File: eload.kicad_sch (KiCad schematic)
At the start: 5 parts, among them J1 Barrel_Jack, Q1 IRF740, U1 MAX4080T

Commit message: Schematics updated
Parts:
- removed U1: MAX4080T, symbol Amplifier_Current:MAX4080T
- added C1, C2, C3: 100nF, symbol Device:C_Small
- added R2: 330K, symbol Device:R_Small
- added R3: 100K, symbol Device:R_Small
- added U1: MCP4725, Package_TO_SOT_SMD:SOT-23-6, symbol Analog_DAC:MCP4725xxx-xCH
- added U2: AD2829, symbol Device:Opamp_Dual
- added U3: STM32F103C8Tx, Package_QFP:LQFP-48_7x7mm_P0.5mm, symbol MCU_ST_STM32F1:STM32F103C8Tx
- R1: symbol Device:R -> Device:R_Small
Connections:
- net Earth: now also R1.2, C1.2, C2.2, C3.2, R3.2, U1.2 (VSS), U1.6 (A0), U2.4 (V-); no longer Q1.3 (S)
- net VCC: now also C1.1, C2.1, C3.1, U1.3 (VDD), U2.8 (V+)
- net VDD: now also Q1.2 (D), R2.1; no longer R1.1
- net at Q1.1 (G): now also U2.1
- new net: Q1.3 (S), R1.1, U2.2 (-)
- new net: U3.23 (VSS), U3.35 (VSS), U3.47 (VSS)
- new net JNRST: U3.7 (NRST)
- new net SCL: U1.5 (SCL), U3.45 (PB8)
- new net SDA: U1.4 (SDA), U3.46 (PB9)
- new net SWCLK: U3.37 (PA14)
- new net SWDIO: U3.34 (PA13)
- new net Vctrl: U1.1 (VOUT), U2.3 (+)
- new net Vsense: R2.2, R3.1, U3.10 (PA0)
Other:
- note added: "15V MAX 12bit ADC 1bit/mV = 4.096V 1:4 division"
- note added: "Voltage Sensing & Current Regulation"
- note removed: "20V/V Gain 1A * 0.1R * 20V/V = 2V max"
- company: (none) -> Denis Bazhenov
- title: (none) -> Bench Electronic Load
- moved on the sheet: HS1, Q1, R1

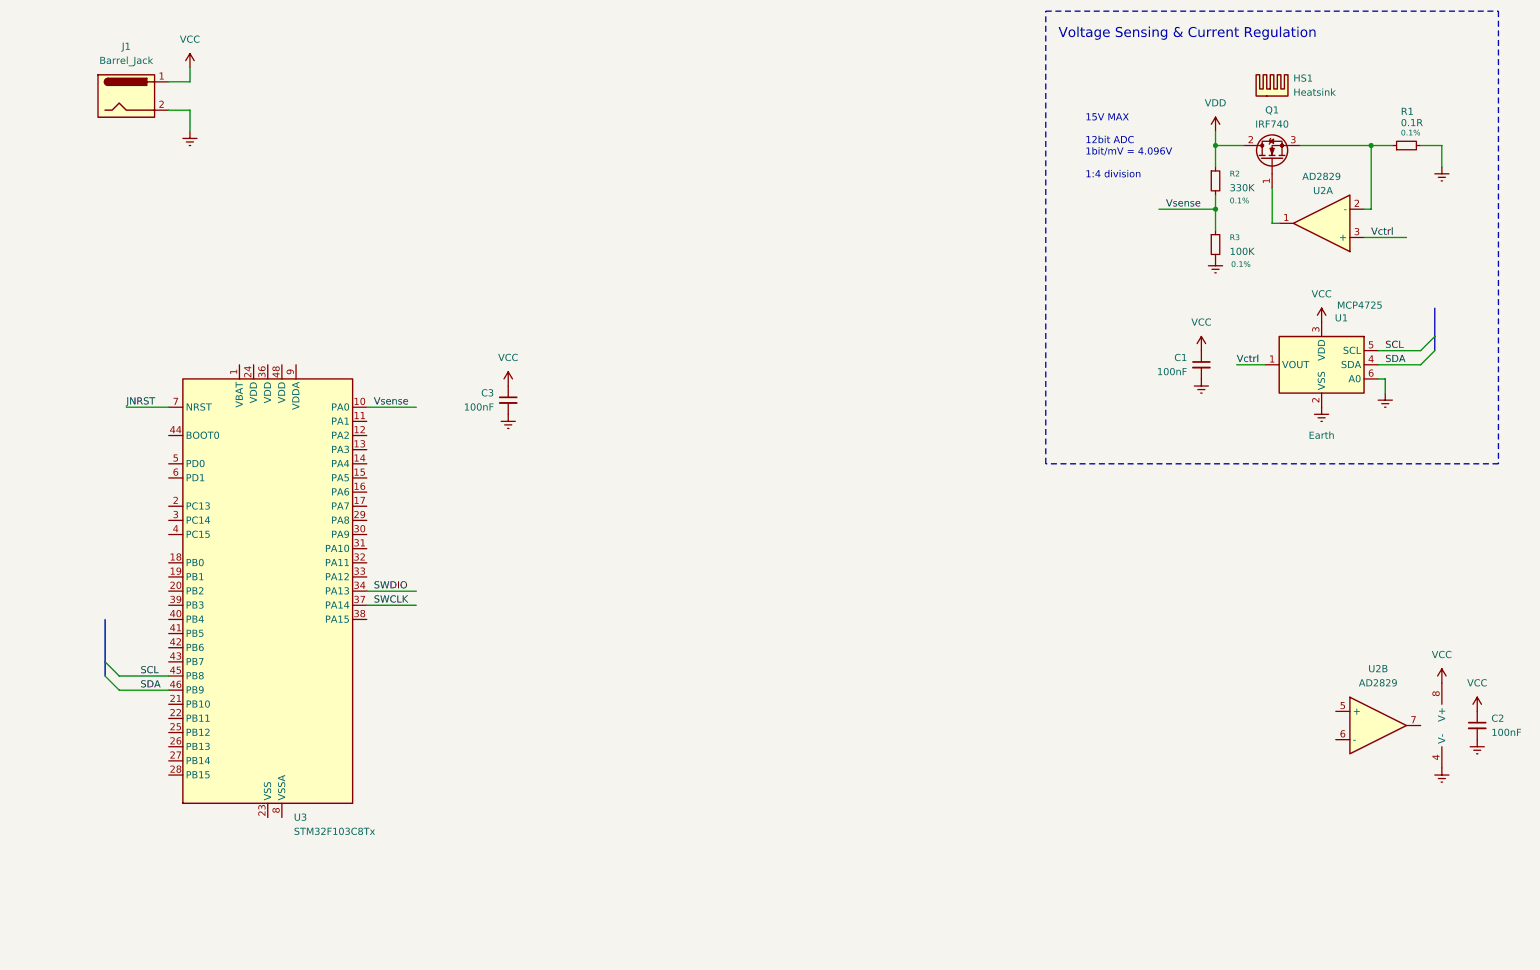
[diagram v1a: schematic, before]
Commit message: Schematics - Power Rail
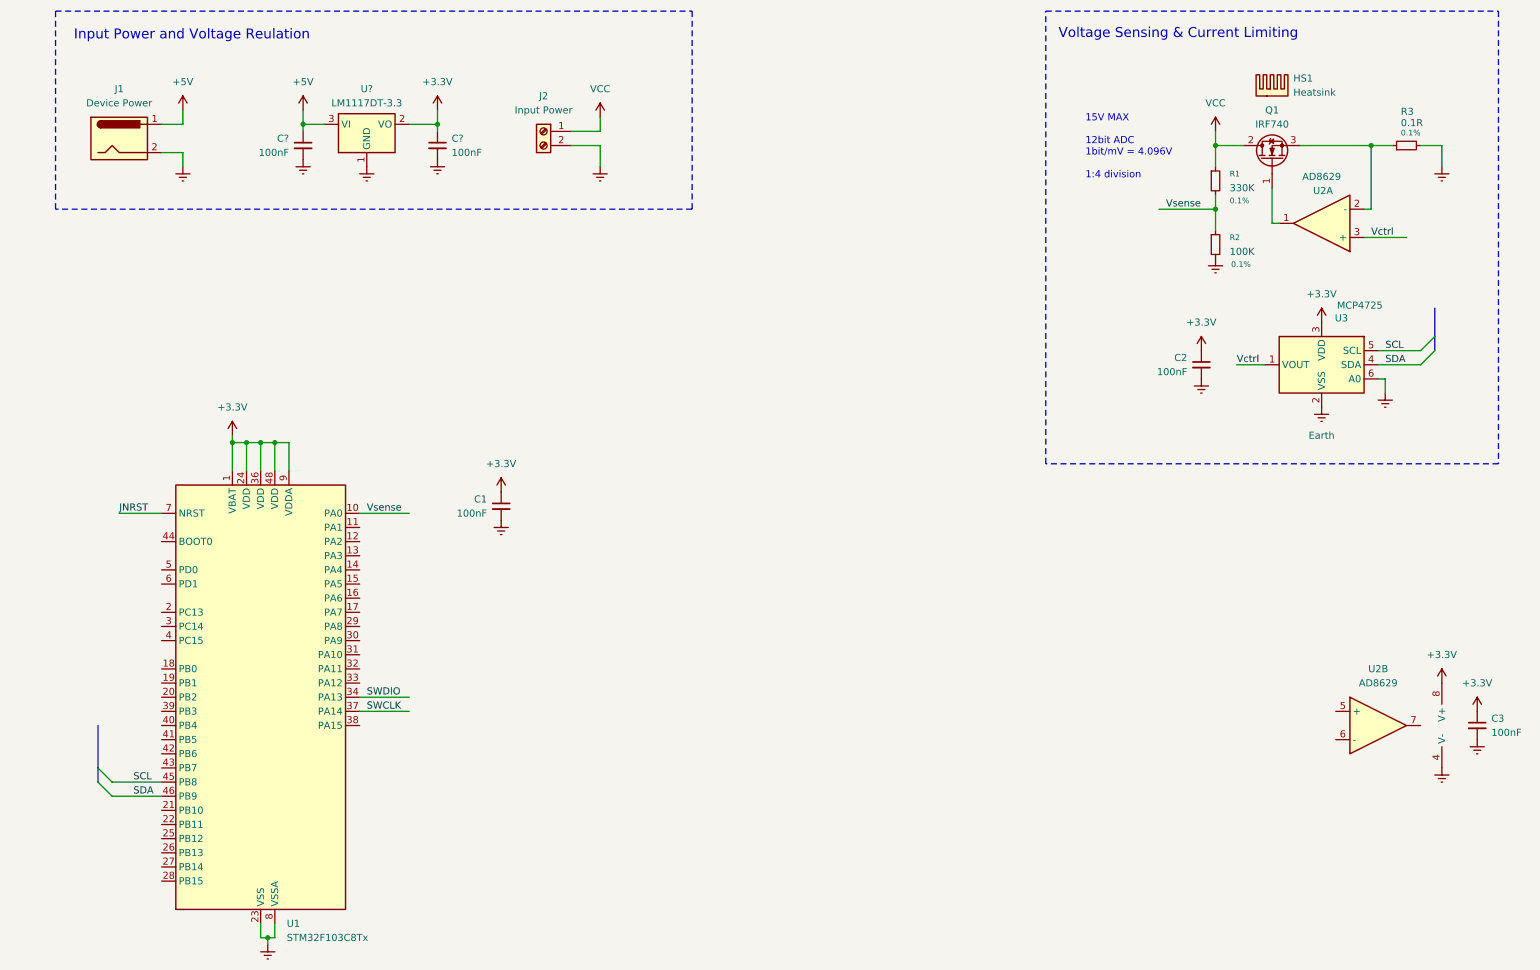
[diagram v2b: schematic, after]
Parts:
- added C? (x2): 100nF, symbol Device:C_Small
- added J2: Input Power, symbol Connector:Screw_Terminal_01x02
- added U?: LM1117DT-3.3, Package_TO_SOT_SMD:TO-252-2, symbol Regulator_Linear:LM1117DT-3.3
- J1: value Barrel_Jack -> Device Power
- U2: value AD2829 -> AD8629
- renumbered C3 to C1, C1 to C2, C2 to C3, R2 to R1, R3 to R2, R1 to R3, U3 to U1, U1 to U3
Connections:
- net VDD is gone; now on net VCC: Q1.2 (D), R1.1
- net Earth: now also U1.23 (VSS), U1.35 (VSS), U1.47 (VSS), U1.8 (VSSA), C?.2, C?.2, J2.2 (Pin_2), U?.1 (GND)
- net VCC: now also J2.1 (Pin_1); no longer C1.1, C2.1, C3.1, J1.1, U2.8 (V+), U3.3 (VDD)
- net +3.3V: now reaches U1.1 (VBAT)
- net +3.3V: now also C1.1, C2.1, C3.1, U1.24 (VDD), U1.36 (VDD), U1.48 (VDD), U1.9 (VDDA), U2.8 (V+), U3.3 (VDD), C?.1, U?.2 (VO)
- new net +5V: C?.1, J1.1, U?.3 (VI)
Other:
- note added: "Input Power and Voltage Reulation"
- note added: "Voltage Sensing & Current Limiting"
- note removed: "Voltage Sensing & Current Regulation"
- moved on the sheet: C1, U1

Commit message: Schematics updated
- fuse added
- rotary encoder connected
- LCD added
- switches added
- minor fixes
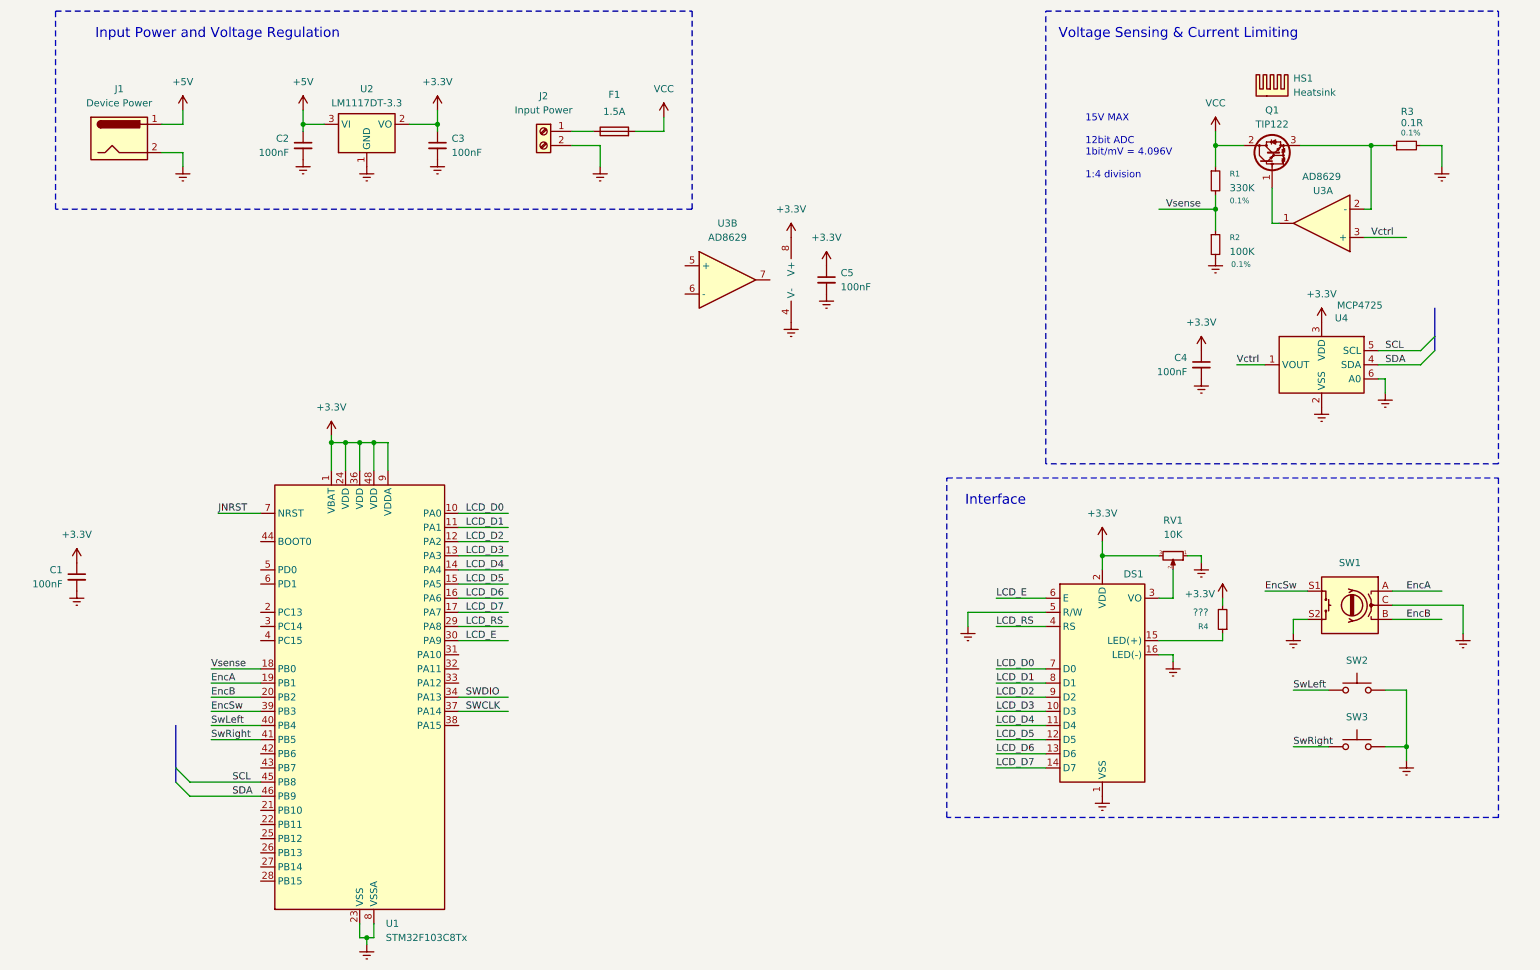
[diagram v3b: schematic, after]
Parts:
- removed Q1: IRF740, Package_TO_SOT_THT:TO-220-3_Vertical, symbol Transistor_FET:IRF740
- added DS1: WC1602A, Display:WC1602A, symbol Display_Character:WC1602A
- added F1: 1.5A, symbol Device:Fuse
- added Q1: TIP122, Package_TO_SOT_THT:TO-220-3_Vertical, symbol Transistor_BJT:TIP122
- added R4: ???, symbol Device:R_Small
- added RV1: 10K, symbol Device:R_Potentiometer_Small
- added SW1: RotaryEncoder_Switch, symbol Device:RotaryEncoder_Switch
- added SW2, SW3: SW_Push, symbol Switch:SW_Push
- gave numbers to parts that had none: 3
- renumbered C2 to C4, C3 to C5, U2 to U3, U3 to U4
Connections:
- net +3.3V: now also DS1.2 (VDD), R4.2, RV1.3
- net Earth: now also DS1.1 (VSS), DS1.16 (LED(-)), DS1.5 (R/W), RV1.1, SW1.C, SW1.S2, SW2.2, SW3.2
- net VCC: now also F1.2, Q1.2 (C); no longer J2.1 (Pin_1)
- net Vsense: now also U1.18 (PB0); no longer U1.10 (PA0)
- net at U3.1: now also Q1.1 (B)
- net at R3.1, U3.2 (-): now also Q1.3 (E)
- net LCD_D1: now reaches U1.11 (PA1)
- net LCD_D1: now also DS1.8 (D1)
- net LCD_D2: now reaches U1.12 (PA2)
- net LCD_D2: now also DS1.9 (D2)
- net LCD_D3: now reaches U1.13 (PA3)
- net LCD_D3: now also DS1.10 (D3)
- net LCD_D4: now reaches U1.14 (PA4)
- net LCD_D4: now also DS1.11 (D4)
- net LCD_D5: now reaches U1.15 (PA5)
- net LCD_D5: now also DS1.12 (D5)
- net LCD_D6: now reaches U1.16 (PA6)
- net LCD_D6: now also DS1.13 (D6)
- net LCD_D7: now reaches U1.17 (PA7)
- net LCD_D7: now also DS1.14 (D7)
- net EncA: now reaches U1.19 (PB1)
- net EncA: now also SW1.A
- net EncB: now reaches U1.20 (PB2)
- net EncB: now also SW1.B
- net LCD_RS: now reaches U1.29 (PA8)
- net LCD_RS: now also DS1.4 (RS)
- net LCD_E: now reaches U1.30 (PA9)
- net LCD_E: now also DS1.6 (E)
- net EncSw: now reaches U1.39 (PB3)
- net EncSw: now also SW1.S1
- net SwLeft: now reaches U1.40 (PB4)
- net SwLeft: now also SW2.1
- net SwRight: now reaches U1.41 (PB5)
- net SwRight: now also SW3.1
- new net: DS1.3 (VO), RV1.2
- new net: DS1.15 (LED(+)), R4.1
- new net: F1.1, J2.1 (Pin_1)
- new net LCD_D0: DS1.7 (D0), U1.10 (PA0)
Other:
- note added: "Input Power and Voltage Regulation"
- note added: "Interface"
- note removed: "Input Power and Voltage Reulation"
- moved on the sheet: C1, C5, U1, U3B

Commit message: Changes to schematics
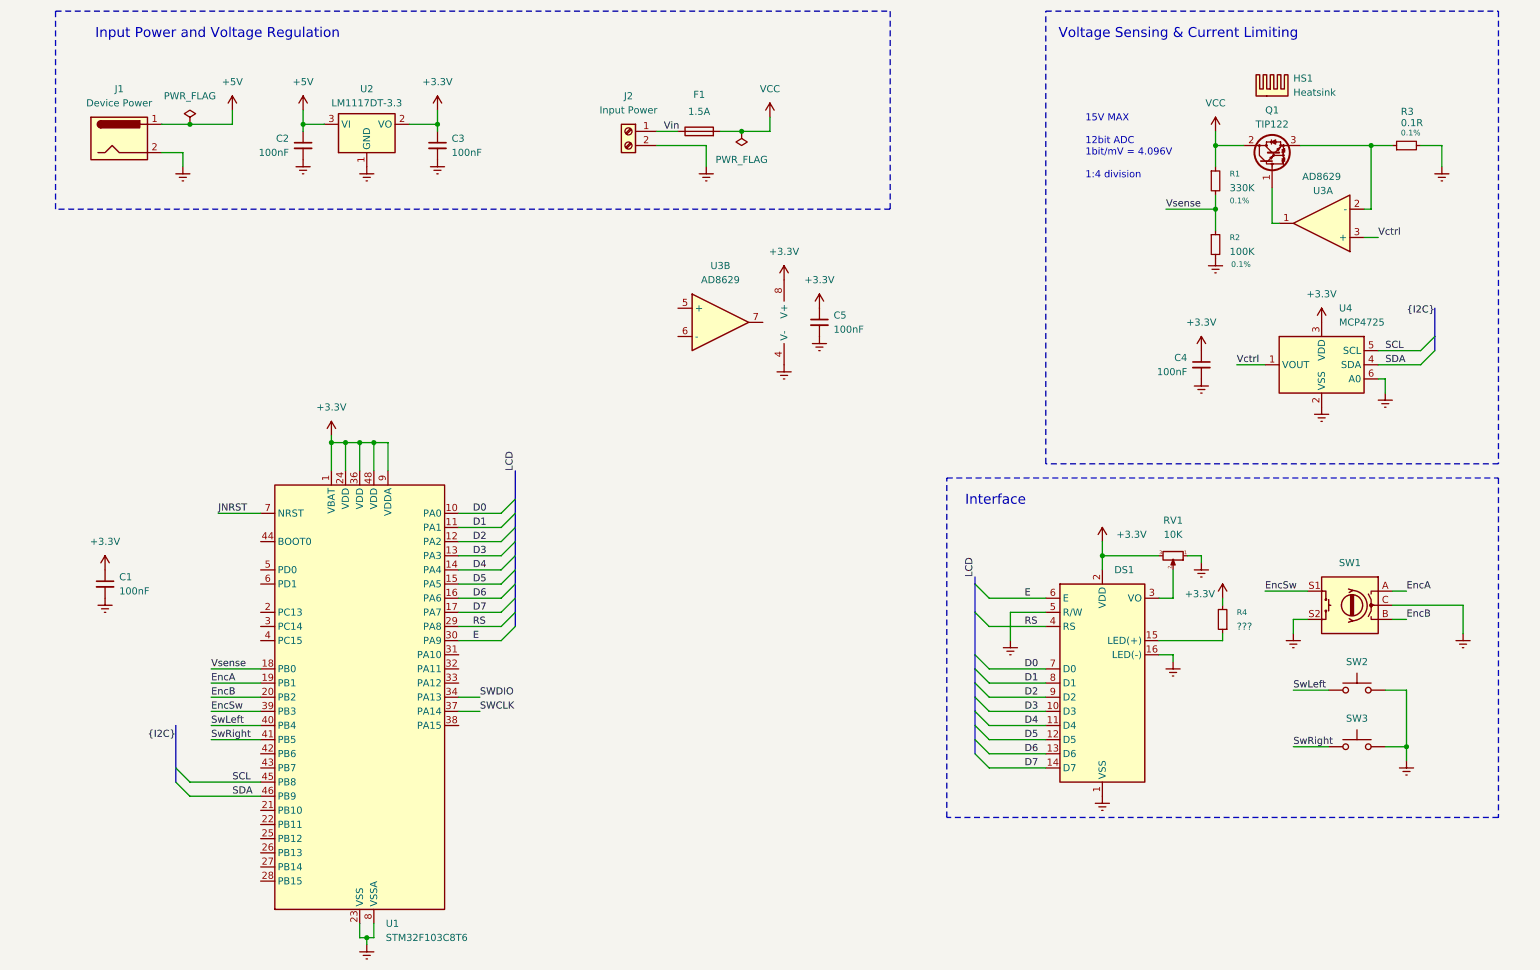
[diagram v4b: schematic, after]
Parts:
- U1: value STM32F103C8Tx -> STM32F103C8T6
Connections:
- net Vin: now reaches F1.1, J2.1 (Pin_1)
- net LCD_D0 renamed D0
- net LCD_D1 renamed D1
- net LCD_D2 renamed D2
- net LCD_D3 renamed D3
- net LCD_D4 renamed D4
- net LCD_D5 renamed D5
- net LCD_D6 renamed D6
- net LCD_D7 renamed D7
- net LCD_E renamed E
- net LCD_RS renamed RS
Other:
- moved on the sheet: C1, C5, F1, J2, U3B

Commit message: Working on ERC checks
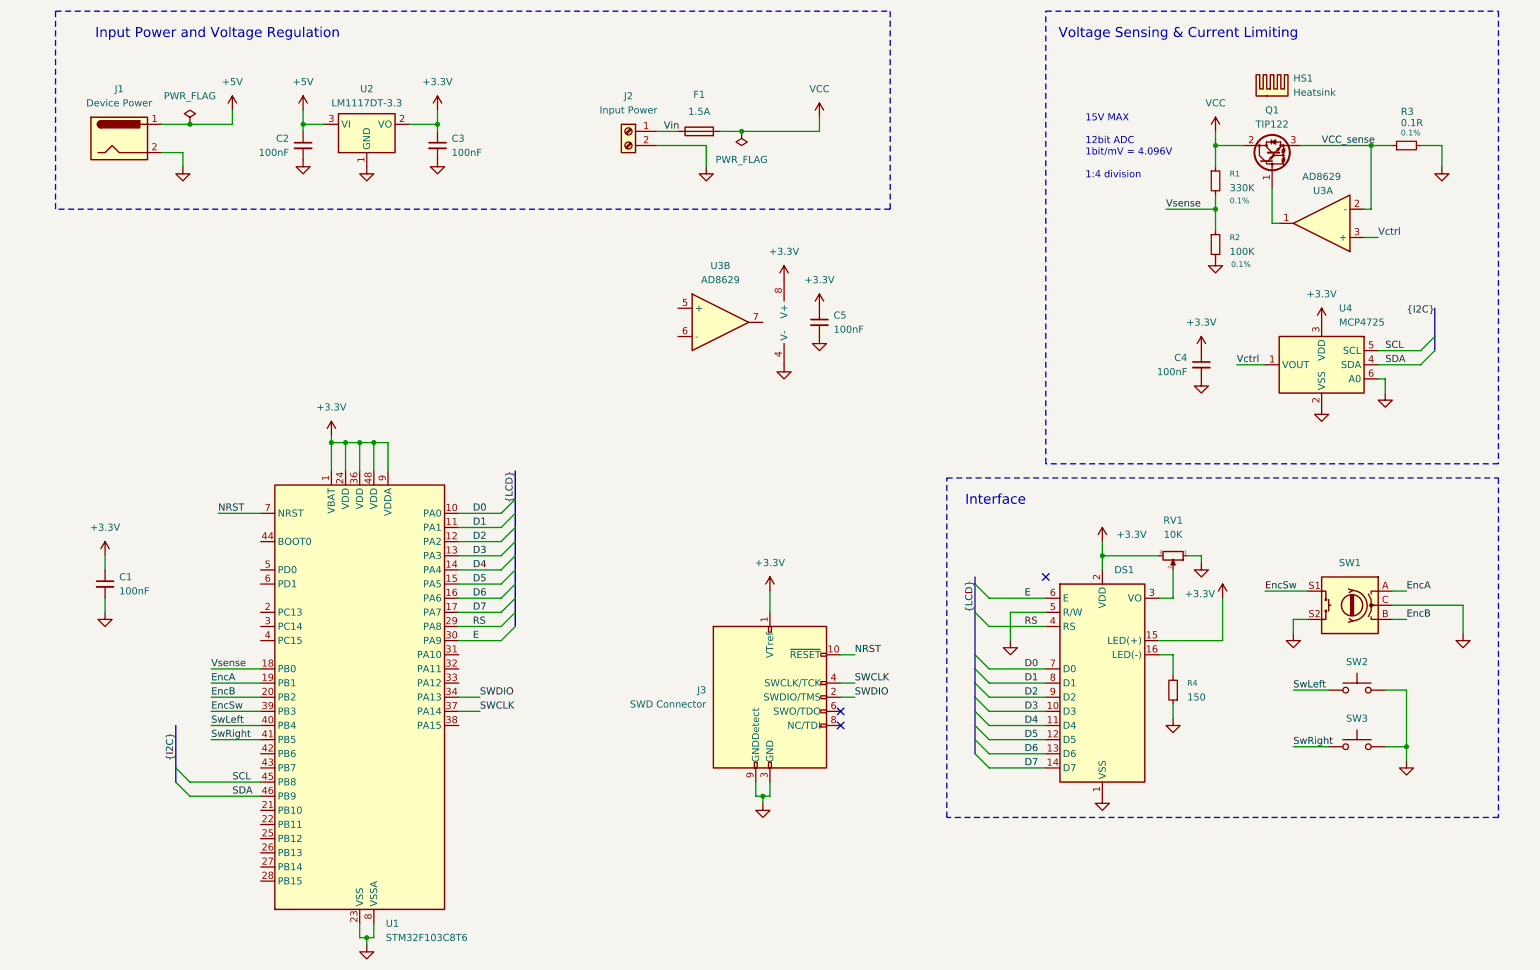
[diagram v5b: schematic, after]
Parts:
- added J3: SWD Connector, Connector_PinHeader_1.27mm:PinHeader_2x07_P1.27mm_Horizontal, symbol Connector:Conn_ARM_JTAG_SWD_10
- R4: value ??? -> 150
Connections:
- net +3.3V: now also DS1.15 (LED(+)), J3.1 (VTref); no longer R4.2
- net SWCLK: now also J3.4 (SWCLK/TCK)
- net SWDIO: now also J3.2 (SWDIO/TMS)
- net VCC_sense: now reaches Q1.3 (E), R3.1, U3.2 (-)
- net GND: now reaches R4.1
- net GND: now also C1.2, C2.2, C3.2, C4.2, C5.2, DS1.1 (VSS), DS1.5 (R/W), J1.2, J2.2 (Pin_2), R2.2, R3.2, RV1.1, SW1.C, SW1.S2, SW2.2, SW3.2, U1.23 (VSS), U1.35 (VSS), U1.47 (VSS), U1.8 (VSSA), U2.1 (GND), U3.4 (V-), U4.2 (VSS), U4.6 (A0), J3.3 (GND), J3.5 (GND), J3.9 (GNDDetect); no longer DS1.15 (LED(+))
- removed net Earth: C1.2, C2.2, C3.2, C4.2, C5.2, DS1.1 (VSS), DS1.16 (LED(-)), DS1.5 (R/W), J1.2, J2.2 (Pin_2), R2.2, R3.2, RV1.1, SW1.C, SW1.S2, SW2.2, SW3.2, U1.23 (VSS), U1.35 (VSS), U1.47 (VSS), U1.8 (VSSA), U2.1 (GND), U3.4 (V-), U4.2 (VSS), U4.6 (A0)
- net JNRST renamed NRST
- net NRST: now also J3.10 (~{RESET})
- new net: DS1.16 (LED(-)), R4.2
- no-connect marks 0 -> 3
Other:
- moved on the sheet: R4

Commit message: SWD header
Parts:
- removed J3: SWD Connector, Connector_PinHeader_1.27mm:PinHeader_2x07_P1.27mm_Horizontal, symbol Connector:Conn_ARM_JTAG_SWD_10
- added C6: 100nF, symbol Device:C_Small
- added J3: SWD Header, Connector_IDC:IDC-Header_2x05_P2.54mm_Vertical, symbol kicad:SWD Header
- renumbered C5 to C4, C4 to C5, R4 to R1, R1 to R2, R2 to R3, R3 to R4
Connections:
- net +3.3V: now also J3.1 (VCC)
- net GND: now also C6.2, J3.3 (GND), J3.5 (GND), J3.9 (GND)
- net SWCLK: now also J3.4 (SWCLK)
- net SWDIO: now also J3.2 (SWDIO)
- net NRST renamed ~{RESET}
- net ~{RESET}: now also C6.1, J3.10 (RESET)
- no-connect marks 3 -> 2

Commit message: Changing encoder pins to PB10/11
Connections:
- net EncA: now also U1.21 (PB10); no longer U1.19 (PB1)
- net EncB: now also U1.22 (PB11); no longer U1.20 (PB2)
- net EncSw: now also U1.19 (PB1); no longer U1.39 (PB3)

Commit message: Remote unneded buttons for now
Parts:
- removed SW2, SW3: SW_Push, symbol Switch:SW_Push
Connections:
- net SwRight is gone; now on net EncSw: U1.41 (PB5)
- net EncSw: no longer U1.19 (PB1)
- net SwLeft: no longer names the net of U1.40 (PB4)
